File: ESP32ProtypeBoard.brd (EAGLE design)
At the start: 78.7 x 80 mm, 102 parts, among them IC1 SOIC-8, IC2 SI4431BDY, IC4 LMC555*, Q1 MMBT3904*, Q2 MMBT3904, Q3 MMBT3904, U2 ESP-WROOM-32

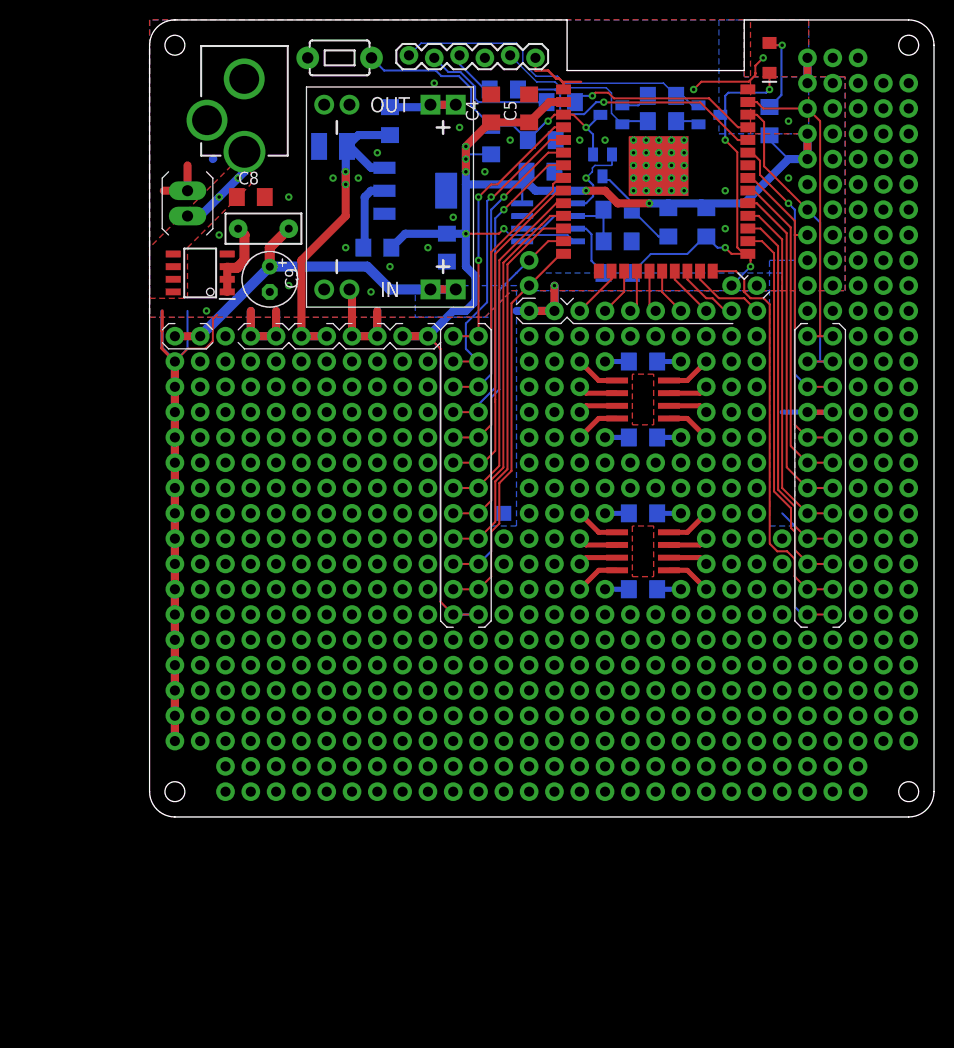
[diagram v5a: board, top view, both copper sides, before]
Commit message: Fixed silk
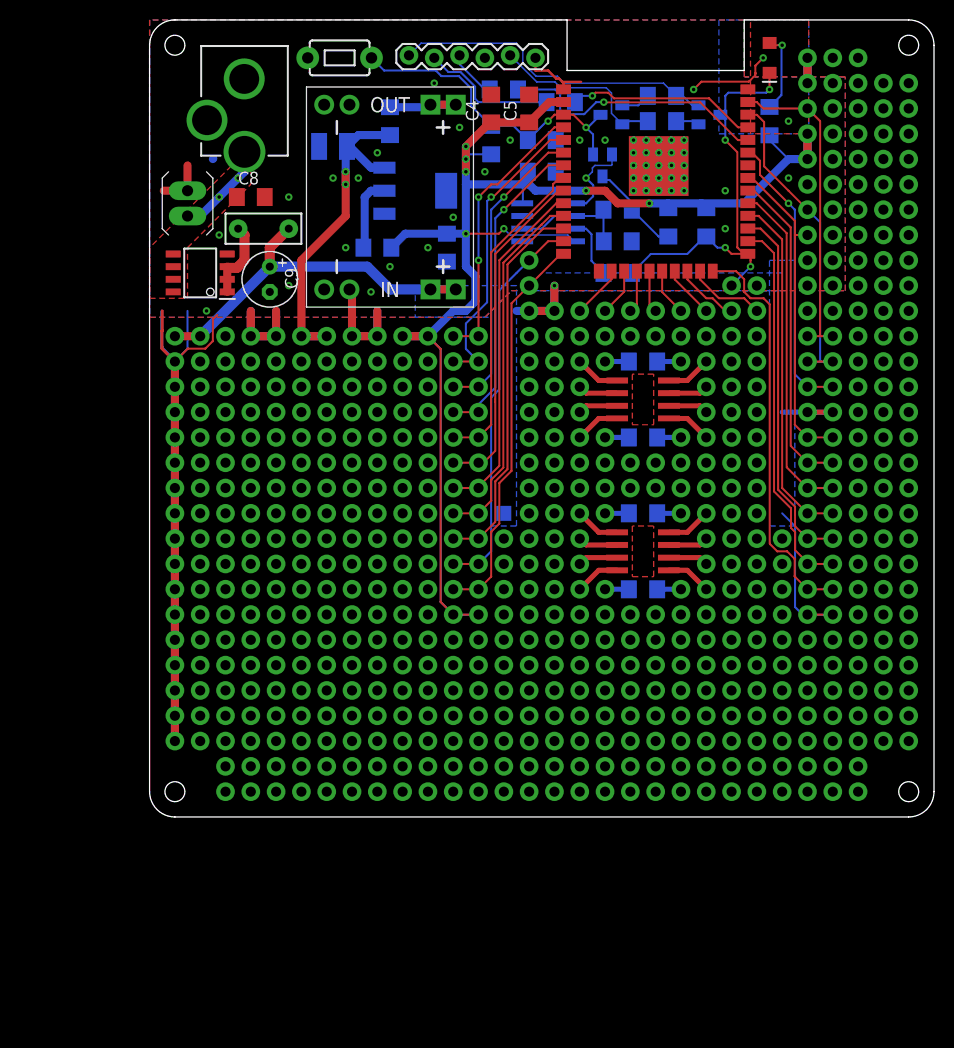
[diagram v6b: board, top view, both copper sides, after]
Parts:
- moved C10 0.13 mm to (39.4, 64.8)
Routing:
- net GND: track 201.9 -> 204.4 mm
- net +3V3: track 178.1 -> 177.2 mm

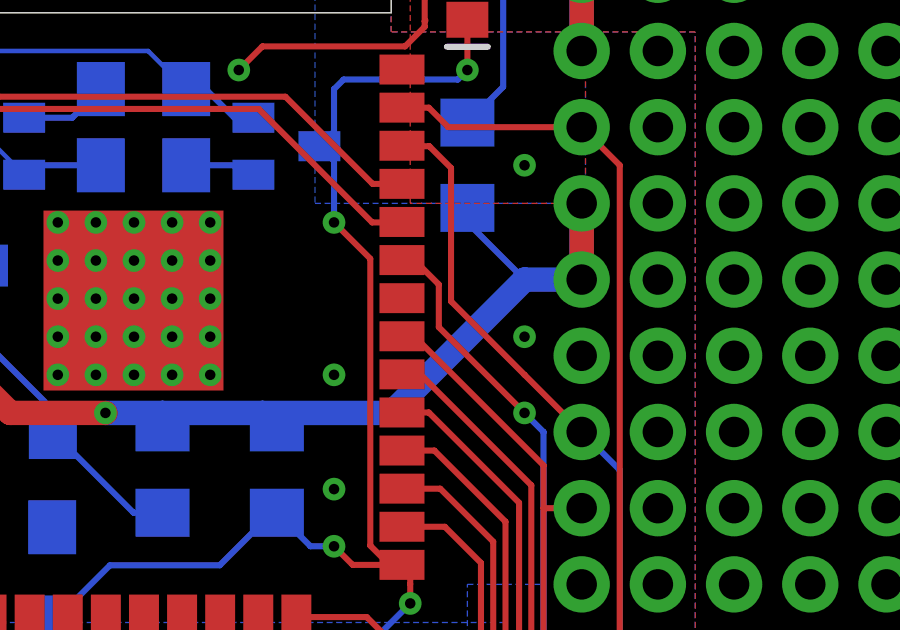
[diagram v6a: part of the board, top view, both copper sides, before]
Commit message: More silk tuning
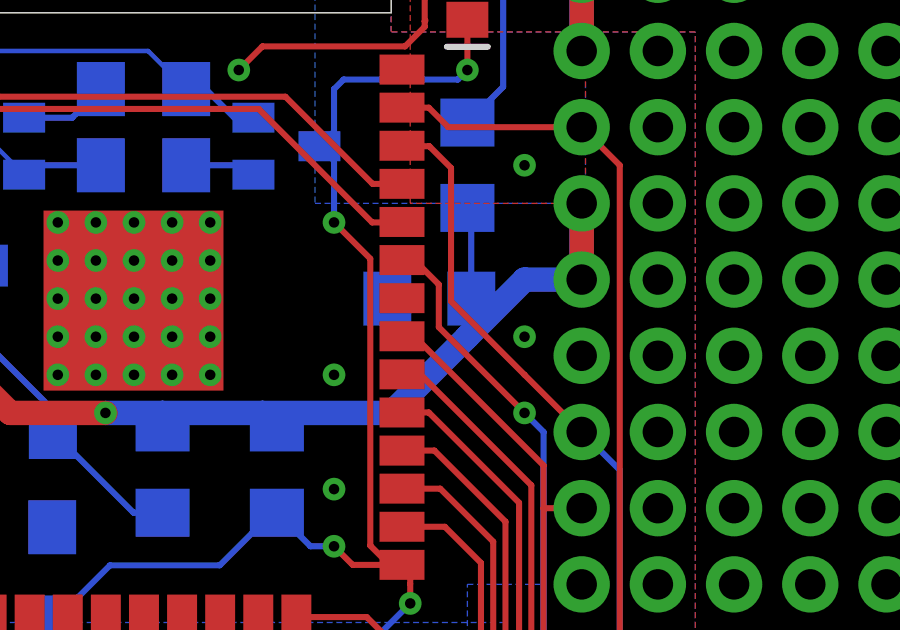
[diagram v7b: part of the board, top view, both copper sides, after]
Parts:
- added C7: (1uF), rcl:C1206
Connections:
- net +3V3: now also C7.1
- net GND: now also C7.2
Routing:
- net +3V3: track 177.2 -> 178.9 mm

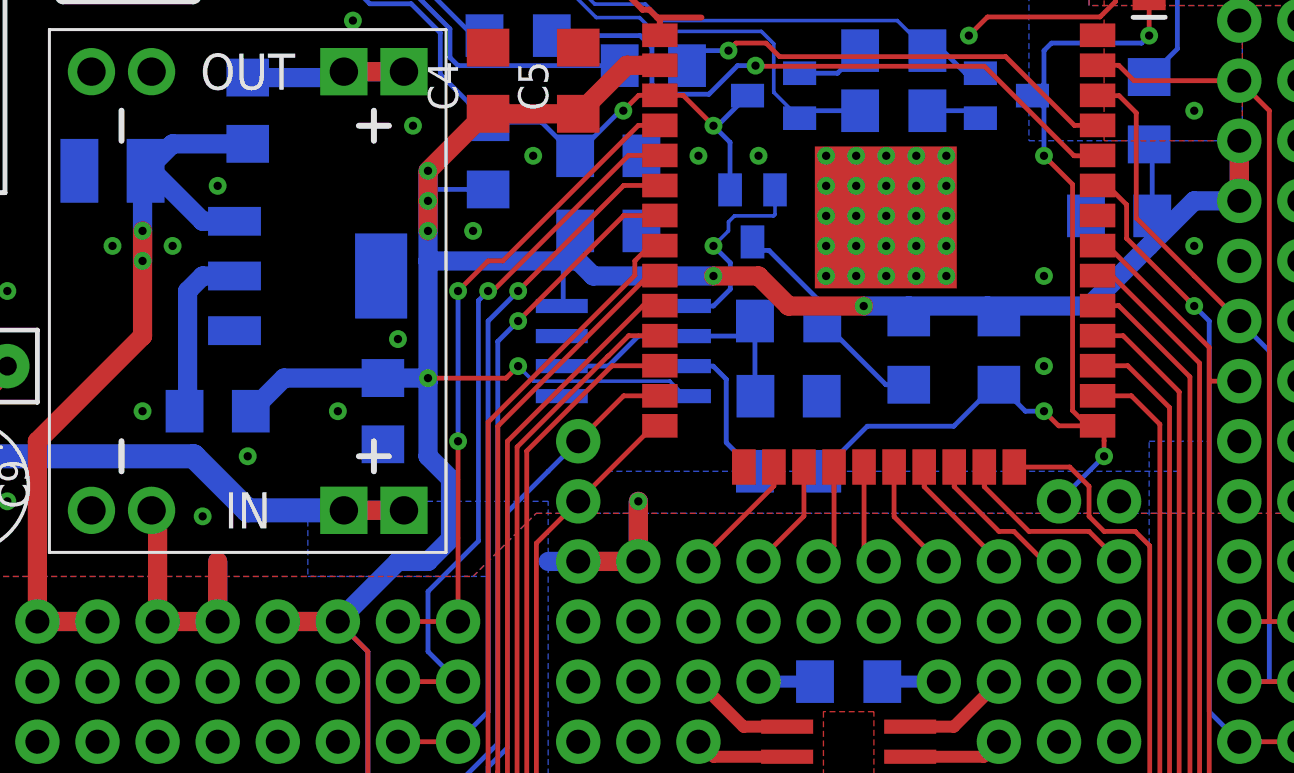
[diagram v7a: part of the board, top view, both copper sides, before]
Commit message: Fixed some stubs
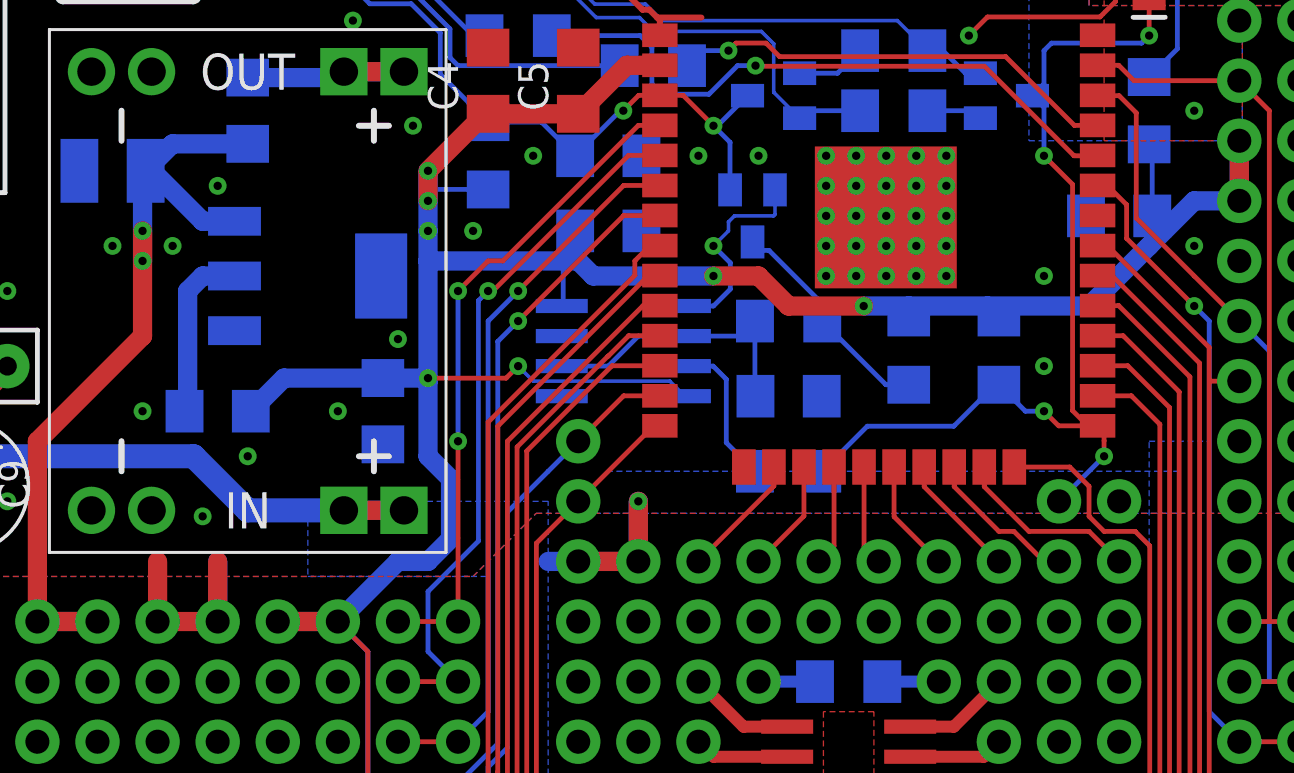
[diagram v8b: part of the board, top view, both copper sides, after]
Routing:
- net GND: track 204.4 -> 201.5 mm
- net +3V3: track 178.9 -> 176.8 mm
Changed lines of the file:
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@@
 <drawing>
 <settings>
-<setting alwaysvectorfont="no"/>
+<setting alwaysvectorfont="yes"/>
 <setting verticaltext="up"/>
 </settings>
@@
 <layer number="25" name="tNames" color="7" fill="1" visible="no" active="yes"/>
 <layer number="26" name="bNames" color="7" fill="1" visible="no" active="yes"/>
-<layer number="27" name="tValues" color="7" fill="1" visible="no" active="yes"/>
+<layer number="27" name="tValues" color="7" fill="1" visible="yes" active="yes"/>
 <layer number="28" name="bValues" color="7" fill="1" visible="yes" active="yes"/>
 <layer number="29" name="tStop" color="7" fill="3" visible="no" active="yes"/>
@@
 <contactref element="J31" pad="4"/>
 <contactref element="IO2" pad="1"/>
-<wire x1="20.32" y1="51.435" x2="20.32" y2="48.26" width="0.762" layer="16"/>
+<wire x1="20.32" y1="50.8" x2="20.32" y2="48.26" width="0.762" layer="16"/>
 <wire x1="20.32" y1="48.26" x2="22.86" y2="48.26" width="0.762" layer="16"/>
 <polygon width="0.254" layer="1" isolate="0.4064" rank="4">
@@
 <contactref element="Q1" pad="2"/>
 <via x="13.97" y="62.23" extent="1-16" drill="0.35"/>
-<wire x1="20.32" y1="52.705" x2="20.066" y2="52.959" width="0.8128" layer="1"/>
-<wire x1="20.32" y1="48.26" x2="20.32" y2="52.705" width="0.8128" layer="1"/>
+<wire x1="20.32" y1="48.26" x2="20.32" y2="50.8" width="0.8128" layer="1"/>
 <contactref element="C5" pad="2"/>
 <contactref element="C4" pad="2"/>
@@
 <contactref element="R5" pad="1"/>
 <contactref element="C3" pad="1"/>
-<wire x1="31.75" y1="64.77" x2="31.75" y2="65.888" width="0.8128" layer="16"/>
 <via x="31.75" y="64.77" extent="1-16" drill="0.35"/>
 <via x="31.75" y="66.04" extent="1-16" drill="0.35"/>
-<wire x1="31.75" y1="64.77" x2="31.75" y2="66.04" width="0.8128" layer="1"/>
 <wire x1="31.75" y1="66.04" x2="31.75" y2="67.18" width="0.8128" layer="1"/>
 <wire x1="34.29" y1="69.72" x2="38.1" y2="69.72" width="0.8128" layer="1"/>
@@
 <wire x1="38.1" y1="63.5" x2="38.735" y2="62.865" width="0.8128" layer="16"/>
 <wire x1="38.735" y1="62.865" x2="43.815" y2="62.865" width="0.8128" layer="16"/>
-<wire x1="37.84" y1="63.875" x2="37.465" y2="63.5" width="0.8128" layer="16"/>
 <via x="43.815" y="62.865" extent="1-16" drill="0.35"/>
 <wire x1="43.815" y1="62.865" x2="45.72" y2="62.865" width="0.8128" layer="1"/>
@@
 <wire x1="66.04" y1="66.04" x2="66.04" y2="68.58" width="0.8128" layer="16"/>
 <wire x1="66.04" y1="68.58" x2="66.04" y2="66.04" width="0.8128" layer="1"/>
-<wire x1="62.23" y1="67.945" x2="62.23" y2="68.428" width="0.2032" layer="16"/>
 <wire x1="34.29" y1="66.523" x2="31.75" y2="66.523" width="0.2032" layer="16"/>
 <wire x1="31.75" y1="66.523" x2="31.75" y2="66.04" width="0.2032" layer="16"/>
 <wire x1="37.405" y1="61.595" x2="37.465" y2="61.655" width="0.2032" layer="16"/>
 <wire x1="37.465" y1="61.655" x2="37.465" y2="63.5" width="0.2032" layer="16"/>
-<wire x1="37.465" y1="63.5" x2="37.97" y2="64.005" width="0.2032" layer="16"/>
-<wire x1="37.97" y1="64.005" x2="37.97" y2="64.77" width="0.2032" layer="16"/>
 <contactref element="C7" pad="1"/>
 <wire x1="62.36" y1="65.405" x2="62.36" y2="64.265" width="0.2032" layer="16"/>
@@
 <wire x1="62.36" y1="65.405" x2="62.36" y2="68.298" width="0.2032" layer="16"/>
 <wire x1="62.36" y1="68.298" x2="62.23" y2="68.428" width="0.2032" layer="16"/>
+<wire x1="37.465" y1="63.5" x2="37.465" y2="64.265" width="0.2032" layer="16"/>
+<wire x1="37.465" y1="64.265" x2="37.97" y2="64.77" width="0.2032" layer="16"/>
+<wire x1="31.75" y1="64.77" x2="31.75" y2="66.04" width="0.8128" layer="16"/>
 </signal>
 <signal name="EN">
